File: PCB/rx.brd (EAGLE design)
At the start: 97.8 x 64.8 mm, 8 parts

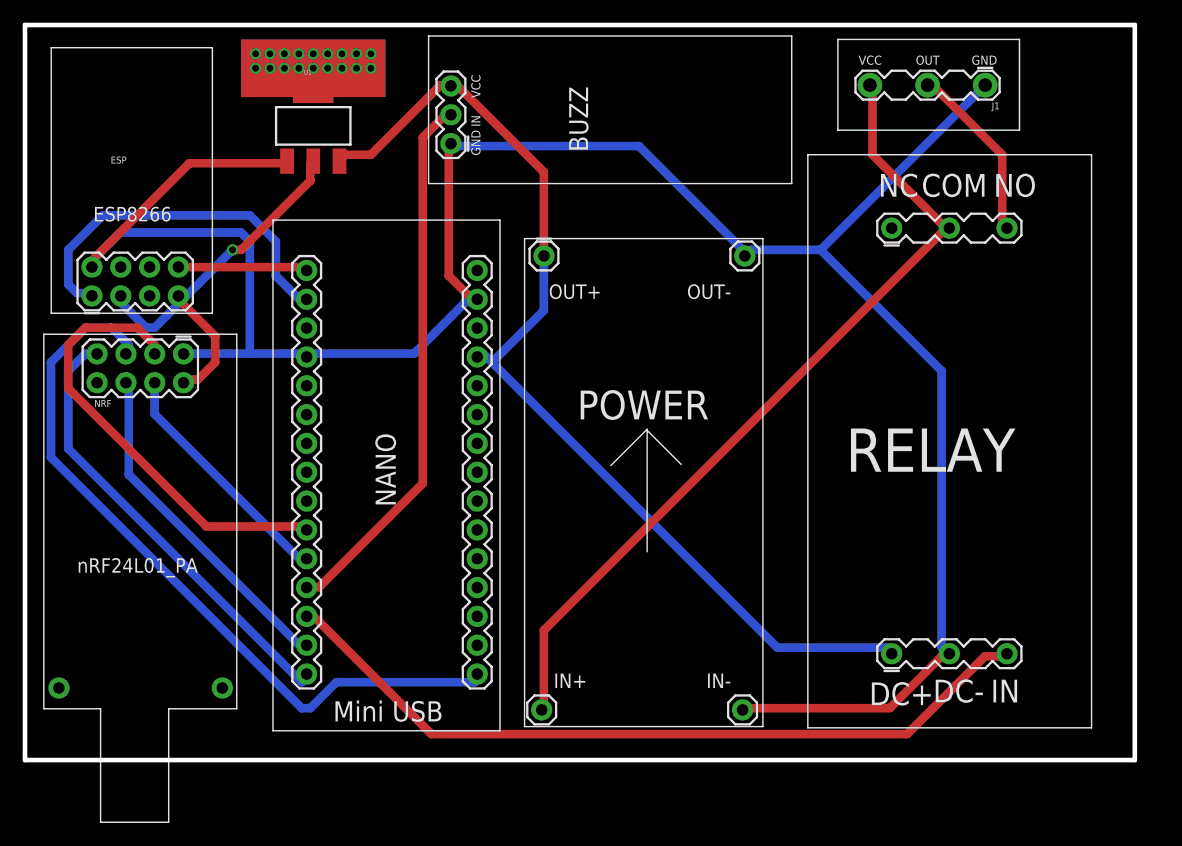
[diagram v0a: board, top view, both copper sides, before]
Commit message: add 315mhz
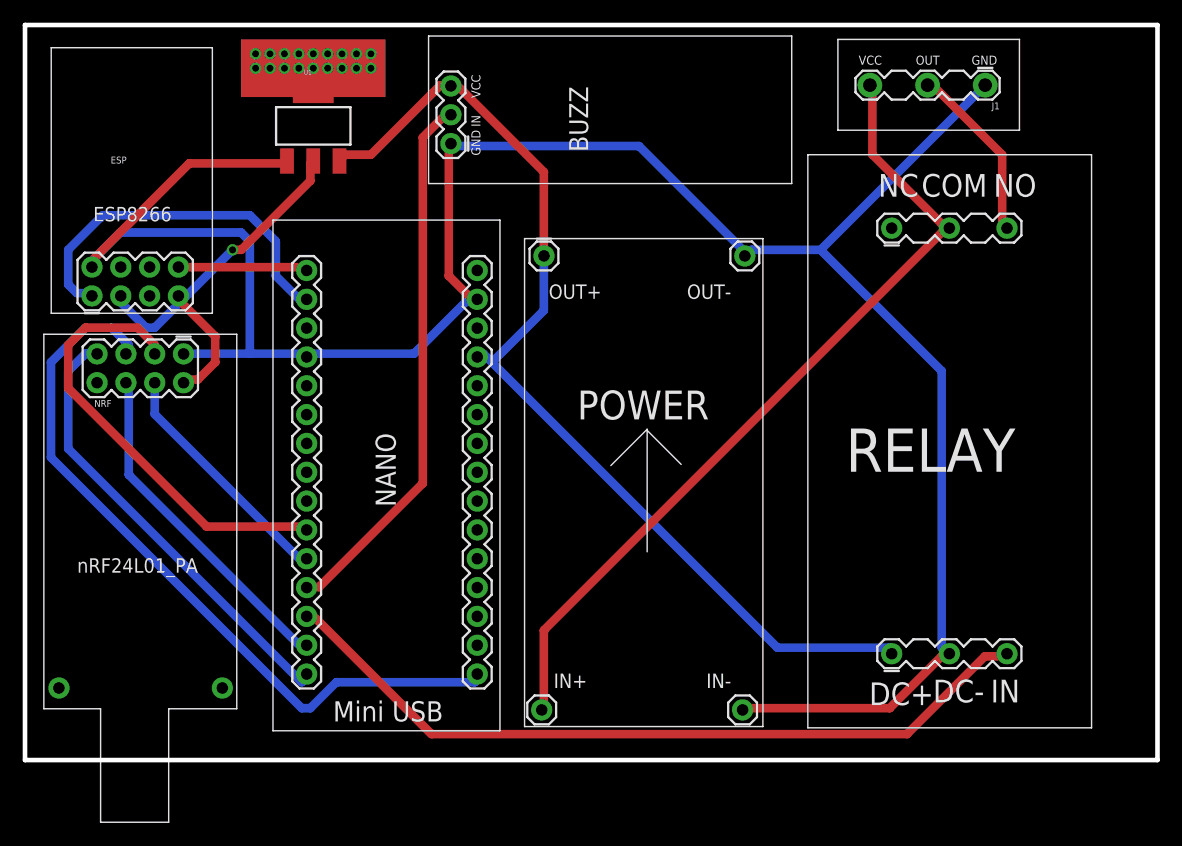
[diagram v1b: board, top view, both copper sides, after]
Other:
- board size 97.8 x 64.8 mm -> 99.8 x 64.8 mm
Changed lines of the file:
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@@
 <setting verticaltext="up"/>
 </settings>
-<grid distance="0.05" unitdist="inch" unit="mm" style="lines" multiple="1" display="yes" altdistance="0.025" altunitdist="inch" altunit="inch"/>
+<grid distance="1" unitdist="mm" unit="mm" style="lines" multiple="1" display="yes" altdistance="0.025" altunitdist="inch" altunit="inch"/>
 <layers>
 <layer number="1" name="Top" color="4" fill="1" visible="yes" active="yes"/>
@@
 <plain>
 <wire x1="0" y1="0" x2="0" y2="64.77" width="0.4064" layer="20"/>
-<wire x1="0" y1="64.77" x2="97.79" y2="64.77" width="0.4064" layer="20"/>
-<wire x1="97.79" y1="64.77" x2="97.79" y2="0" width="0.4064" layer="20"/>
-<wire x1="97.79" y1="0" x2="0" y2="0" width="0.4064" layer="20"/>
+<wire x1="0" y1="64.77" x2="99.79" y2="64.77" width="0.4064" layer="20"/>
+<wire x1="99.79" y1="64.77" x2="99.79" y2="0" width="0.4064" layer="20"/>
+<wire x1="99.79" y1="0" x2="0" y2="0" width="0.4064" layer="20"/>
 <rectangle x1="19.05" y1="58.42" x2="31.75" y2="63.5" layer="1"/>
 <rectangle x1="19.05" y1="58.42" x2="31.75" y2="63.5" layer="16"/>

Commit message: web prepare
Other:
- board size 99.8 x 64.8 mm -> 93.8 x 63.8 mm
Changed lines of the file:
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@@
 <board>
 <plain>
-<wire x1="0" y1="0" x2="0" y2="64.77" width="0.4064" layer="20"/>
-<wire x1="0" y1="64.77" x2="99.79" y2="64.77" width="0.4064" layer="20"/>
-<wire x1="99.79" y1="64.77" x2="99.79" y2="0" width="0.4064" layer="20"/>
-<wire x1="99.79" y1="0" x2="0" y2="0" width="0.4064" layer="20"/>
+<wire x1="1" y1="1" x2="1" y2="64.77" width="0.4064" layer="20"/>
+<wire x1="1" y1="64.77" x2="94.79" y2="64.77" width="0.4064" layer="20"/>
+<wire x1="94.79" y1="64.77" x2="94.79" y2="1" width="0.4064" layer="20"/>
+<wire x1="94.79" y1="1" x2="1" y2="1" width="0.4064" layer="20"/>
 <rectangle x1="19.05" y1="58.42" x2="31.75" y2="63.5" layer="1"/>
 <rectangle x1="19.05" y1="58.42" x2="31.75" y2="63.5" layer="16"/>
